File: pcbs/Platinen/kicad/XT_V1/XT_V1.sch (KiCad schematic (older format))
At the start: 77 parts, among them J1 Conn_01x04, J10 TBL009-500-02GY-2GY, J2 Conn_01x02, J3 Conn_01x02, J4 Conn_02x03_Odd_Even, J5 Conn_02x05_Odd_Even, J6 Conn_02x05_Odd_Even, J7 TBL009-500-02GY-2GY, J8 TBL009-500-02GY-2GY, J9 TBL009-500-02GY-2GY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

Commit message: bugfixes on PCBs
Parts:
- J10, J7, J8, J9: symbol KiCAD_personalized:TBL009-500-02GY-2GY -> XT_V1-rescue:TBL009-500-02GY-2GY-KiCAD_personalized
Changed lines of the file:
@@
 $EndComp
 $Comp
-L KiCAD_personalized:TBL009-500-02GY-2GY J7
+L XT_V1-rescue:TBL009-500-02GY-2GY-KiCAD_personalized J7
 U 1 1 60CB663B
 P 10600 1050
@@
 $EndComp
 $Comp
-L KiCAD_personalized:TBL009-500-02GY-2GY J8
+L XT_V1-rescue:TBL009-500-02GY-2GY-KiCAD_personalized J8
 U 1 1 60D3A938
 P 10600 2250
@@
 $EndComp
 $Comp
-L KiCAD_personalized:TBL009-500-02GY-2GY J9
+L XT_V1-rescue:TBL009-500-02GY-2GY-KiCAD_personalized J9
 U 1 1 60D41E13
 P 10600 3450
@@
 $EndComp
 $Comp
-L KiCAD_personalized:TBL009-500-02GY-2GY J10
+L XT_V1-rescue:TBL009-500-02GY-2GY-KiCAD_personalized J10
 U 1 1 60D4DB35
 P 10600 4600

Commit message: Redesign XT V1
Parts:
- removed Q5, Q7: BT136-500, Package_TO_SOT_THT:TO-220-3_Vertical, symbol Triac_Thyristor:BT136-500
- removed U6, U8: MOC3043M, Package_DIP:DIP-6_W8.89mm_SMDSocket_LongPads, symbol Relay_SolidState:MOC3043M
- added D1, D2: SM4007, Diode_SMD:D_MELF, symbol Diode:SM4007
- added Q10, Q9: BT136-500, Package_TO_SOT_THT:TO-220-3_Vertical, symbol Triac_Thyristor:BT136-500
- added Q5, Q7: BC846, Package_TO_SOT_SMD:SOT-23, symbol Transistor_BJT:BC846
- added R32: 330, Resistor_SMD:R_0805_2012Metric_Pad1.20x1.40mm_HandSolder, symbol Device:R
- added R33, R34: 56k, Resistor_SMD:R_MELF_MMB-0207, symbol Device:R
- added R35, R36, R37: 68, Resistor_SMD:R_0805_2012Metric_Pad1.20x1.40mm_HandSolder, symbol Device:R
- added U10, U9: MOC3043M, Package_DIP:DIP-6_W8.89mm_SMDSocket_LongPads, symbol Relay_SolidState:MOC3043M
- added U6, U8: TLP291, Package_SO:SOIC-4_4.55x2.6mm_P1.27mm, symbol Isolator:TLP291
- R17, R18: value max 360 -> 1k
- R20, R22: value 360 -> max 360
- R23: value 360 -> 1k
- R24: value 330 -> 1k
- R26, R27: value 330 -> 360
- R28: value 68 -> 360
- R30, R31: value 68 -> 330
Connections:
- net +3V3: now also R13.1, R14.1
- net CH2: now also R15.2; no longer R13.2
- net CH3: now also R17.2; no longer R14.2
- net CH4: now also R18.2; no longer R15.2
- net GND: now also Q5.2 (E), Q7.2 (E)
- net VCC: now also R20.2, R22.2, U6.4, U8.4; no longer R17.2, R18.2
- net at U5.4: now also Q6.3 (G), R25.2; no longer R24.2
- net at U5.6: now also R21.2; no longer R20.2
- net at J7.1, J7.2: now also Q6.2 (A2), Q8.2 (A2), R21.1, R26.1, R29.1, D1.2 (A), R35.1, U6.2; no longer R20.1, R28.1
- net at J7.3, J7.4: now also R33.1; no longer C15.2, R24.1
- net at C15.1: now also R35.2; no longer R28.2
- net ZC1: now reaches U3.33 (PA12)
- net ZC1: now also Q2.3 (C), R13.2
- net ZC2: now reaches U3.38 (PA15)
- net ZC2: now also Q3.3 (C), R14.2
- net at R17.1: now also Q5.1 (B)
- net at C16.2, Q6.1 (A1), R25.1: now also J8.1, J8.2; no longer J8.3, J8.4
- net at U7.1: now also R19.1; no longer R18.1
- net at U7.2: now also Q4.3 (C); no longer Q3.3 (C)
- net at U7.4: now also Q8.3 (G), R30.2; no longer R26.2
- net at U7.6: now also R26.2; no longer R22.2
- net at J9.1, J9.2: now also R27.1, R28.1, D2.2 (A), Q10.2 (A2), Q9.2 (A2), R36.1, R37.1, U8.2; no longer R22.1, R30.1
- net at J9.3, J9.4: now also R34.1; no longer C17.2, R26.1
- net at C17.1: now also R36.2; no longer R30.2
- net at R27.2: now also U9.6; no longer Q8.3 (G)
- net at R23.2: now also Q2.1 (B)
- net at J10.1, J10.2, R31.1: now also C17.2, Q9.1 (A1); no longer Q8.2 (A2), R23.1
- net at C18.2, J10.3, J10.4: now also Q10.1 (A1), R32.1; no longer Q8.1 (A1), R27.1
- net at R31.2: now also Q9.3 (G), U9.4; no longer C18.1
- net at Q3.1 (B): now also R24.2; no longer R14.1
- new net: C15.2, J8.3, J8.4, Q8.1 (A1), R30.1
- new net: D1.1 (K), R33.2, U6.1
- new net: R23.1, U6.3
- new net: R20.1, U9.1
- new net: Q5.3 (C), U9.2
- new net: D2.1 (K), R34.2, U8.1
- new net: R24.1, U8.3
- new net: R22.1, U10.1
- new net: Q7.3 (C), U10.2
- new net: Q10.3 (G), R32.2, U10.4
- new net: R28.2, U10.6
- new net: Q7.1 (B), R18.1
- new net: C18.1, R37.2
- no-connect marks 18 -> 16
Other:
- note added: "AC 1"
- note added: "Caps: C0805C103JARACTU (M)\n56k: VIT ZC207 56K (R)"
- note removed: "Caps: C0805C103JARACTU"
- moved on the sheet: C11, C13, C16, C5, C7, J5, J6, J8, Q1, Q6, R12, R16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

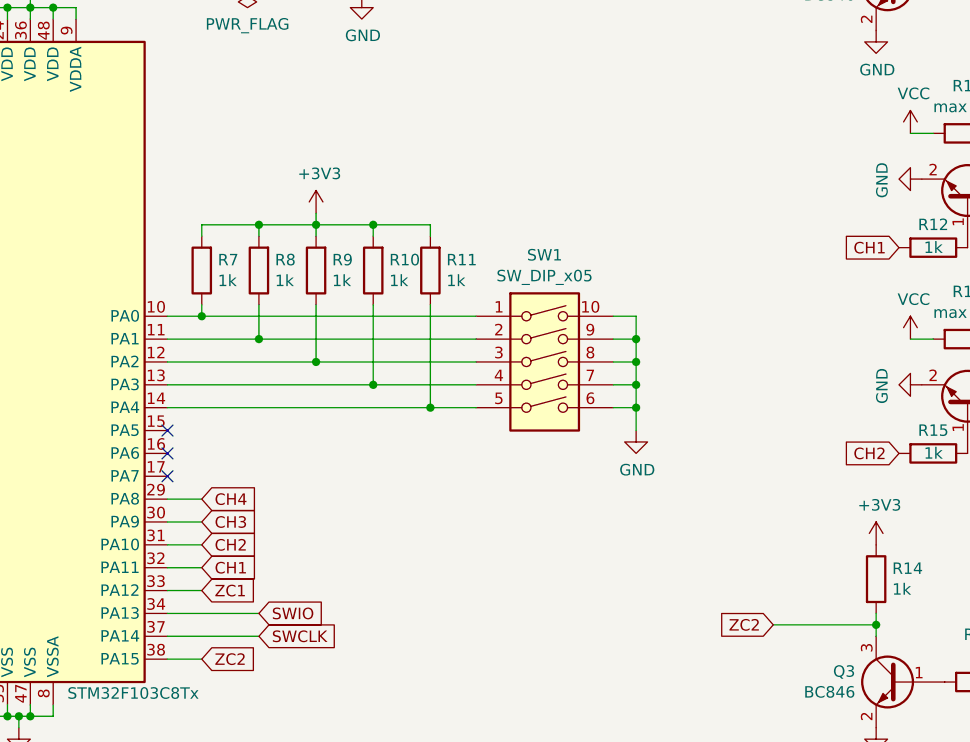
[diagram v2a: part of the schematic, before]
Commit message: fix error in Schematic
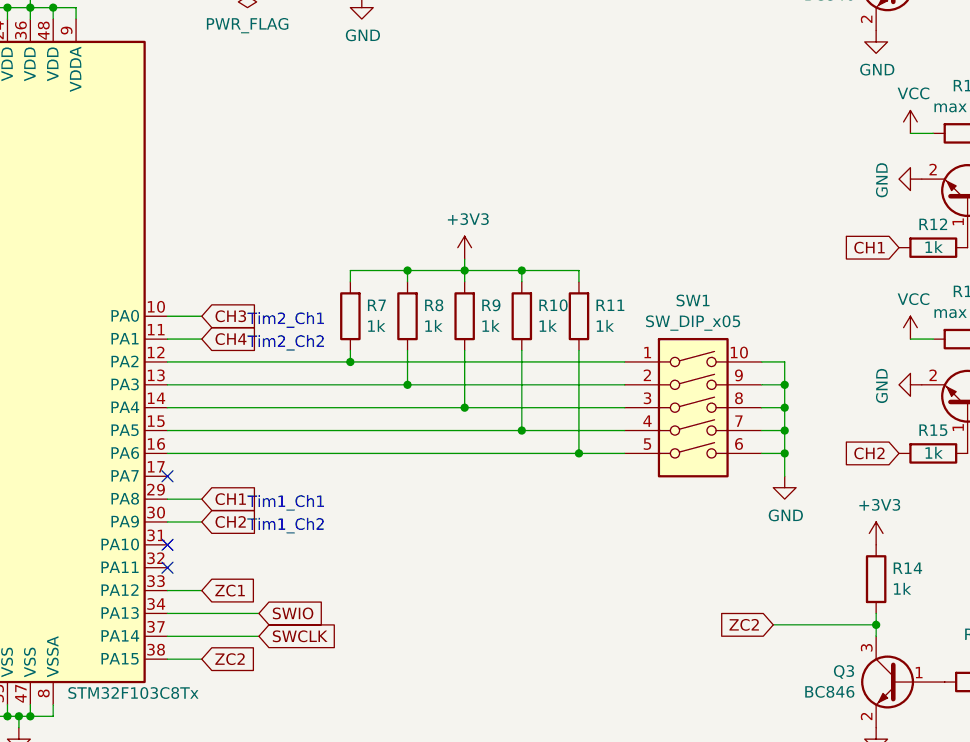
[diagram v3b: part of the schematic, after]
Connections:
- net CH1: now also U3.29 (PA8); no longer U3.32 (PA11)
- net CH2: now also U3.30 (PA9); no longer U3.31 (PA10)
- net CH3: now also U3.10 (PA0); no longer U3.30 (PA9)
- net CH4: now also U3.11 (PA1); no longer U3.29 (PA8)
- net at R7.1, SW1.1: now also U3.12 (PA2); no longer U3.10 (PA0)
- net at R8.1, SW1.2: now also U3.13 (PA3); no longer U3.11 (PA1)
- net at R9.1, SW1.3: now also U3.14 (PA4); no longer U3.12 (PA2)
- net at R10.1, SW1.4: now also U3.15 (PA5); no longer U3.13 (PA3)
- net at R11.1, SW1.5: now also U3.16 (PA6); no longer U3.14 (PA4)
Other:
- note added: "Tim1_Ch1\n"
- note added: "Tim1_Ch2"
- note added: "Tim2_Ch1"
- note added: "Tim2_Ch2"
- moved on the sheet: R10, R11, R7, R8, R9, SW1
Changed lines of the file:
@@
 L Switch:SW_DIP_x05 SW1
 U 1 1 60CE03DB
-P 5700 2950
-F 0 "SW1" H 5700 3417 50  0000 C CNN
-F 1 "SW_DIP_x05" H 5700 3326 50  0000 C CNN
-F 2 "Button_Switch_THT:SW_DIP_SPSTx05_Slide_6.7x14.26mm_W7.62mm_P2.54mm_LowProfile" H 5700 2950 50  0001 C CNN
-F 3 "~" H 5700 2950 50  0001 C CNN
-	1    5700 2950
+P 6350 3150
+F 0 "SW1" H 6350 3617 50  0000 C CNN
+F 1 "SW_DIP_x05" H 6350 3526 50  0000 C CNN
+F 2 "Button_Switch_THT:SW_DIP_SPSTx05_Slide_6.7x14.26mm_W7.62mm_P2.54mm_LowProfile" H 6350 3150 50  0001 C CNN
+F 3 "~" H 6350 3150 50  0001 C CNN
+	1    6350 3150
 	1    0    0    -1
 $EndComp
@@
 L Device:R R7
 U 1 1 60CE5195
-P 4200 2550
-F 0 "R7" H 4130 2504 50  0000 R CNN
-F 1 "1k" H 4130 2595 50  0000 R CNN
-F 2 "Resistor_SMD:R_0805_2012Metric_Pad1.20x1.40mm_HandSolder" V 4130 2550 50  0001 C CNN
-F 3 "~" H 4200 2550 50  0001 C CNN
-	1    4200 2550
+P 4850 2750
+F 0 "R7" H 4780 2704 50  0000 R CNN
+F 1 "1k" H 4780 2795 50  0000 R CNN
+F 2 "Resistor_SMD:R_0805_2012Metric_Pad1.20x1.40mm_HandSolder" V 4780 2750 50  0001 C CNN
+F 3 "~" H 4850 2750 50  0001 C CNN
+	1    4850 2750
 	-1   0    0    1
 $EndComp
@@
 L Device:R R8
 U 1 1 60CE5C03
-P 4450 2550
-F 0 "R8" H 4380 2504 50  0000 R CNN
-F 1 "1k" H 4380 2595 50  0000 R CNN
-F 2 "Resistor_SMD:R_0805_2012Metric_Pad1.20x1.40mm_HandSolder" V 4380 2550 50  0001 C CNN
-F 3 "~" H 4450 2550 50  0001 C CNN
-	1    4450 2550
+P 5100 2750
+F 0 "R8" H 5030 2704 50  0000 R CNN
+F 1 "1k" H 5030 2795 50  0000 R CNN
+F 2 "Resistor_SMD:R_0805_2012Metric_Pad1.20x1.40mm_HandSolder" V 5030 2750 50  0001 C CNN
+F 3 "~" H 5100 2750 50  0001 C CNN
+	1    5100 2750
 	-1   0    0    1
 $EndComp
@@
 L Device:R R9
 U 1 1 60CE60DC
-P 4700 2550
-F 0 "R9" H 4630 2504 50  0000 R CNN
-F 1 "1k" H 4630 2595 50  0000 R CNN
-F 2 "Resistor_SMD:R_0805_2012Metric_Pad1.20x1.40mm_HandSolder" V 4630 2550 50  0001 C CNN
-F 3 "~" H 4700 2550 50  0001 C CNN
-	1    4700 2550
+P 5350 2750
+F 0 "R9" H 5280 2704 50  0000 R CNN
+F 1 "1k" H 5280 2795 50  0000 R CNN
+F 2 "Resistor_SMD:R_0805_2012Metric_Pad1.20x1.40mm_HandSolder" V 5280 2750 50  0001 C CNN
+F 3 "~" H 5350 2750 50  0001 C CNN
+	1    5350 2750
 	-1   0    0    1
 $EndComp
@@
 L Device:R R10
 U 1 1 60CE66C6
-P 4950 2550
-F 0 "R10" H 4880 2504 50  0000 R CNN
-F 1 "1k" H 4880 2595 50  0000 R CNN
-F 2 "Resistor_SMD:R_0805_2012Metric_Pad1.20x1.40mm_HandSolder" V 4880 2550 50  0001 C CNN
-F 3 "~" H 4950 2550 50  0001 C CNN
-	1    4950 2550
+P 5600 2750
+F 0 "R10" H 5530 2704 50  0000 R CNN
+F 1 "1k" H 5530 2795 50  0000 R CNN
+F 2 "Resistor_SMD:R_0805_2012Metric_Pad1.20x1.40mm_HandSolder" V 5530 2750 50  0001 C CNN
+F 3 "~" H 5600 2750 50  0001 C CNN
+	1    5600 2750
 	-1   0    0    1
 $EndComp
@@
 L Device:R R11
 U 1 1 60CE6DC8
-P 5200 2550
-F 0 "R11" H 5130 2504 50  0000 R CNN
-F 1 "1k" H 5130 2595 50  0000 R CNN
-F 2 "Resistor_SMD:R_0805_2012Metric_Pad1.20x1.40mm_HandSolder" V 5130 2550 50  0001 C CNN
-F 3 "~" H 5200 2550 50  0001 C CNN
-	1    5200 2550
+P 5850 2750
+F 0 "R11" H 5780 2704 50  0000 R CNN
+F 1 "1k" H 5780 2795 50  0000 R CNN
+F 2 "Resistor_SMD:R_0805_2012Metric_Pad1.20x1.40mm_HandSolder" V 5780 2750 50  0001 C CNN
+F 3 "~" H 5850 2750 50  0001 C CNN
+	1    5850 2750
 	-1   0    0    1
 $EndComp
@@
 L power:GND #PWR025
 U 1 1 60CEB2F0
-P 6100 3250
-F 0 "#PWR025" H 6100 3000 50  0001 C CNN
-F 1 "GND" H 6105 3077 50  0000 C CNN
-F 2 "" H 6100 3250 50  0001 C CNN
-F 3 "" H 6100 3250 50  0001 C CNN
-	1    6100 3250
-	1    0    0    -1
-$EndComp
-Wire Wire Line
-	6000 2750 6100 2750
-Wire Wire Line
-	6100 2750 6100 2850
-Wire Wire Line
-	6000 3150 6100 3150
-Connection ~ 6100 3150
-Wire Wire Line
-	6100 3150 6100 3250
-Wire Wire Line
-	6000 3050 6100 3050
-Connection ~ 6100 3050
-Wire Wire Line
-	6100 3050 6100 3150
-Wire Wire Line
-	6000 2950 6100 2950
-Connection ~ 6100 2950
-Wire Wire Line
-	6100 2950 6100 3050
-Wire Wire Line
-	6000 2850 6100 2850
-Connection ~ 6100 2850
-Wire Wire Line
-	6100 2850 6100 2950
-Wire Wire Line
-	4050 2750 4200 2750
-Wire Wire Line
-	5400 2850 4450 2850
-Wire Wire Line
-	4050 2950 4700 2950
-Wire Wire Line
-	5400 3050 4950 3050
-Wire Wire Line
-	4050 3150 5200 3150
-Wire Wire Line
-	4200 2700 4200 2750
-Connection ~ 4200 2750
-Wire Wire Line
-	4200 2750 5400 2750
-Wire Wire Line
-	4450 2700 4450 2850
-Connection ~ 4450 2850
-Wire Wire Line
-	4450 2850 4050 2850
-Wire Wire Line
-	4700 2700 4700 2950
-Connection ~ 4700 2950
-Wire Wire Line
-	4700 2950 5400 2950
-Wire Wire Line
-	4950 2700 4950 3050
-Connection ~ 4950 3050
-Wire Wire Line
-	4950 3050 4050 3050
-Wire Wire Line
-	5200 2700 5200 3150
-Connection ~ 5200 3150
-Wire Wire Line
-	5200 3150 5400 3150
+P 6750 3450
+F 0 "#PWR025" H 6750 3200 50  0001 C CNN
+F 1 "GND" H 6755 3277 50  0000 C CNN
+F 2 "" H 6750 3450 50  0001 C CNN
+F 3 "" H 6750 3450 50  0001 C CNN
+	1    6750 3450
+	1    0    0    -1
+$EndComp
+Wire Wire Line
+	6650 2950 6750 2950
+Wire Wire Line
+	6750 2950 6750 3050
+Wire Wire Line
+	6650 3350 6750 3350
+Connection ~ 6750 3350
+Wire Wire Line
+	6750 3350 6750 3450
+Wire Wire Line
+	6650 3250 6750 3250
+Connection ~ 6750 3250
+Wire Wire Line
+	6750 3250 6750 3350
+Wire Wire Line
+	6650 3150 6750 3150
+Connection ~ 6750 3150
+Wire Wire Line
+	6750 3150 6750 3250
+Wire Wire Line
+	6650 3050 6750 3050
+Connection ~ 6750 3050
+Wire Wire Line
+	6750 3050 6750 3150
+Wire Wire Line
+	6050 3050 5100 3050
+Wire Wire Line
+	6050 3250 5600 3250
+Wire Wire Line
+	4850 2900 4850 2950
+Connection ~ 4850 2950
+Wire Wire Line
+	4850 2950 6050 2950
+Wire Wire Line
+	5100 2900 5100 3050
+Connection ~ 5100 3050
+Wire Wire Line
+	5350 2900 5350 3150
+Connection ~ 5350 3150
+Wire Wire Line
+	5350 3150 6050 3150
+Wire Wire Line
+	5600 2900 5600 3250
+Connection ~ 5600 3250
+Wire Wire Line
+	5850 2900 5850 3350
+Connection ~ 5850 3350
+Wire Wire Line
+	5850 3350 6050 3350
 $Comp
 L power:+3V3 #PWR015
 U 1 1 60D02A17
-P 4700 2300
-F 0 "#PWR015" H 4700 2150 50  0001 C CNN
-F 1 "+3V3" H 4715 2473 50  0000 C CNN
-F 2 "" H 4700 2300 50  0001 C CNN
-F 3 "" H 4700 2300 50  0001 C CNN
-	1    4700 2300
-	1    0    0    -1
-$EndComp
-Wire Wire Line
-	4700 2300 4700 2350
-Wire Wire Line
-	4200 2400 4200 2350
-Wire Wire Line
-	4200 2350 4450 2350
-Connection ~ 4700 2350
-Wire Wire Line
-	4700 2350 4700 2400
-Wire Wire Line
-	4700 2350 4950 2350
-Wire Wire Line
-	5200 2350 5200 2400
-Wire Wire Line
-	4950 2400 4950 2350
-Connection ~ 4950 2350
-Wire Wire Line
-	4950 2350 5200 2350
-Wire Wire Line
-	4450 2400 4450 2350
-Connection ~ 4450 2350
-Wire Wire Line
-	4450 2350 4700 2350
+P 5350 2500
+F 0 "#PWR015" H 5350 2350 50  0001 C CNN
+F 1 "+3V3" H 5365 2673 50  0000 C CNN
+F 2 "" H 5350 2500 50  0001 C CNN
+F 3 "" H 5350 2500 50  0001 C CNN
+	1    5350 2500
+	1    0    0    -1
+$EndComp
+Wire Wire Line
+	5350 2500 5350 2550
+Wire Wire Line
+	4850 2600 4850 2550
+Wire Wire Line
+	4850 2550 5100 2550
+Connection ~ 5350 2550
+Wire Wire Line
+	5350 2550 5350 2600
+Wire Wire Line
+	5350 2550 5600 2550
+Wire Wire Line
+	5850 2550 5850 2600
+Wire Wire Line
+	5600 2600 5600 2550
+Connection ~ 5600 2550
+Wire Wire Line
+	5600 2550 5850 2550
+Wire Wire Line
+	5100 2600 5100 2550
+Connection ~ 5100 2550
+Wire Wire Line
+	5100 2550 5350 2550
 $Comp
 L Device:R R29
@@
 	0    1    1    0
 $EndComp
-Text GLabel 4200 3850 2    50   Input ~ 0
+Text GLabel 4200 3550 2    50   Input ~ 0
 CH1
-Text GLabel 4200 3750 2    50   Input ~ 0
+Text GLabel 4200 3650 2    50   Input ~ 0
 CH2
-Text GLabel 4200 3650 2    50   Input ~ 0
+Text GLabel 4200 2750 2    50   Input ~ 0
 CH3
-Text GLabel 4200 3550 2    50   Input ~ 0
+Text GLabel 4200 2850 2    50   Input ~ 0
 CH4
 Text GLabel 7250 2450 0    50   Input ~ 0
 CH1
 Wire Wire Line
+	4050 2850 4200 2850
+Wire Wire Line
+	4050 2750 4200 2750
+Wire Wire Line
+	4050 3650 4200 3650
+Wire Wire Line
 	4050 3550 4200 3550
-Wire Wire Line
-	4050 3650 4200 3650
-Wire Wire Line
-	4050 3750 4200 3750
-Wire Wire Line
-	4050 3850 4200 3850
 Text Notes 9150 3600 0    50   ~ 0
 Galvanische Trennung\nmind. 1,5mm
@@
 NoConn ~ 2750 4250
 NoConn ~ 4050 3450
-NoConn ~ 4050 3350
-NoConn ~ 4050 3250
 $Comp
 L power:+3V3 #PWR026
@@
 	0    -1   -1   0
 $EndComp
+Wire Wire Line
+	4050 2950 4850 2950
+Wire Wire Line
+	4050 3050 5100 3050
+Wire Wire Line
+	4050 3150 5350 3150
+Wire Wire Line
+	4050 3250 5600 3250
+Wire Wire Line
+	4050 3350 5850 3350
+NoConn ~ 4050 3850
+NoConn ~ 4050 3750
+Text Notes 4400 3600 0    50   ~ 0
+Tim1_Ch1\n
+Text Notes 4400 3700 0    50   ~ 0
+Tim1_Ch2
+Text Notes 4400 2900 0    50   ~ 0
+Tim2_Ch2
+Text Notes 4400 2800 0    50   ~ 0
+Tim2_Ch1
 $EndSCHEMATC
